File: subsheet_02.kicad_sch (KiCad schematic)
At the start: 1 part, among them J2 GATE_ARRAY_MO5_V1_SOCKET

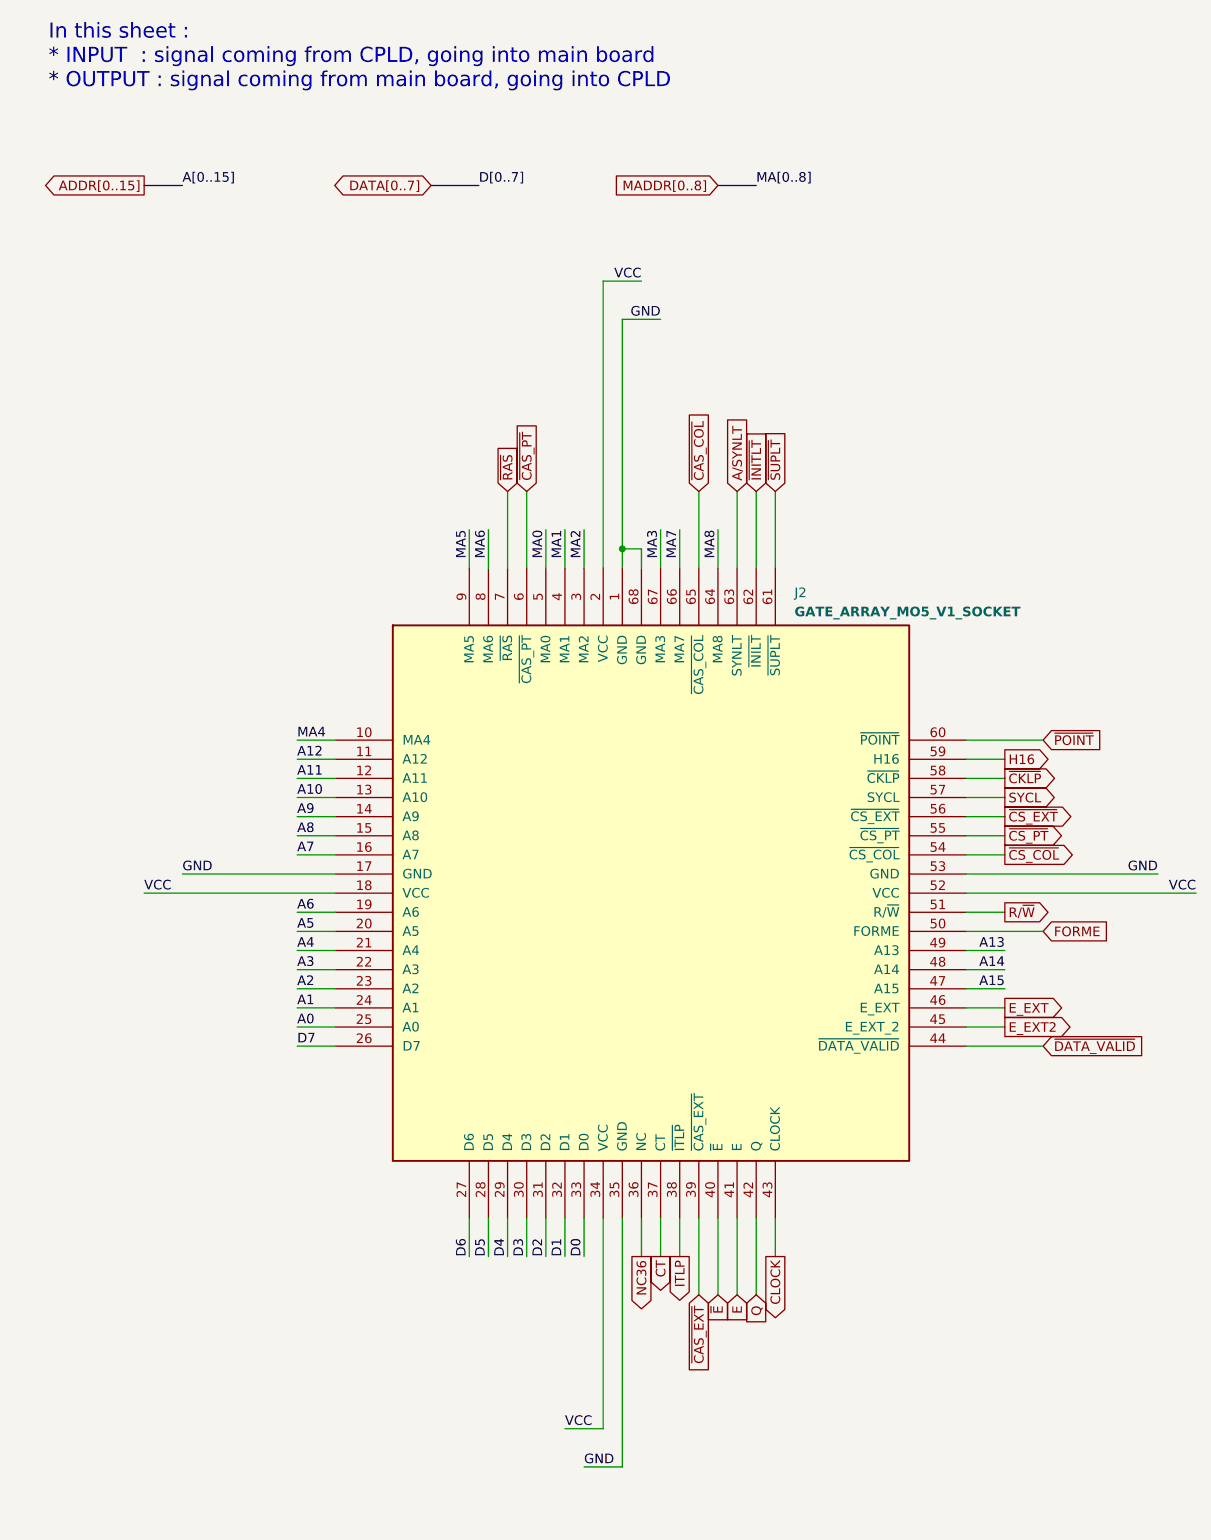
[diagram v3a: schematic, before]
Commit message: schematics : put power symbols
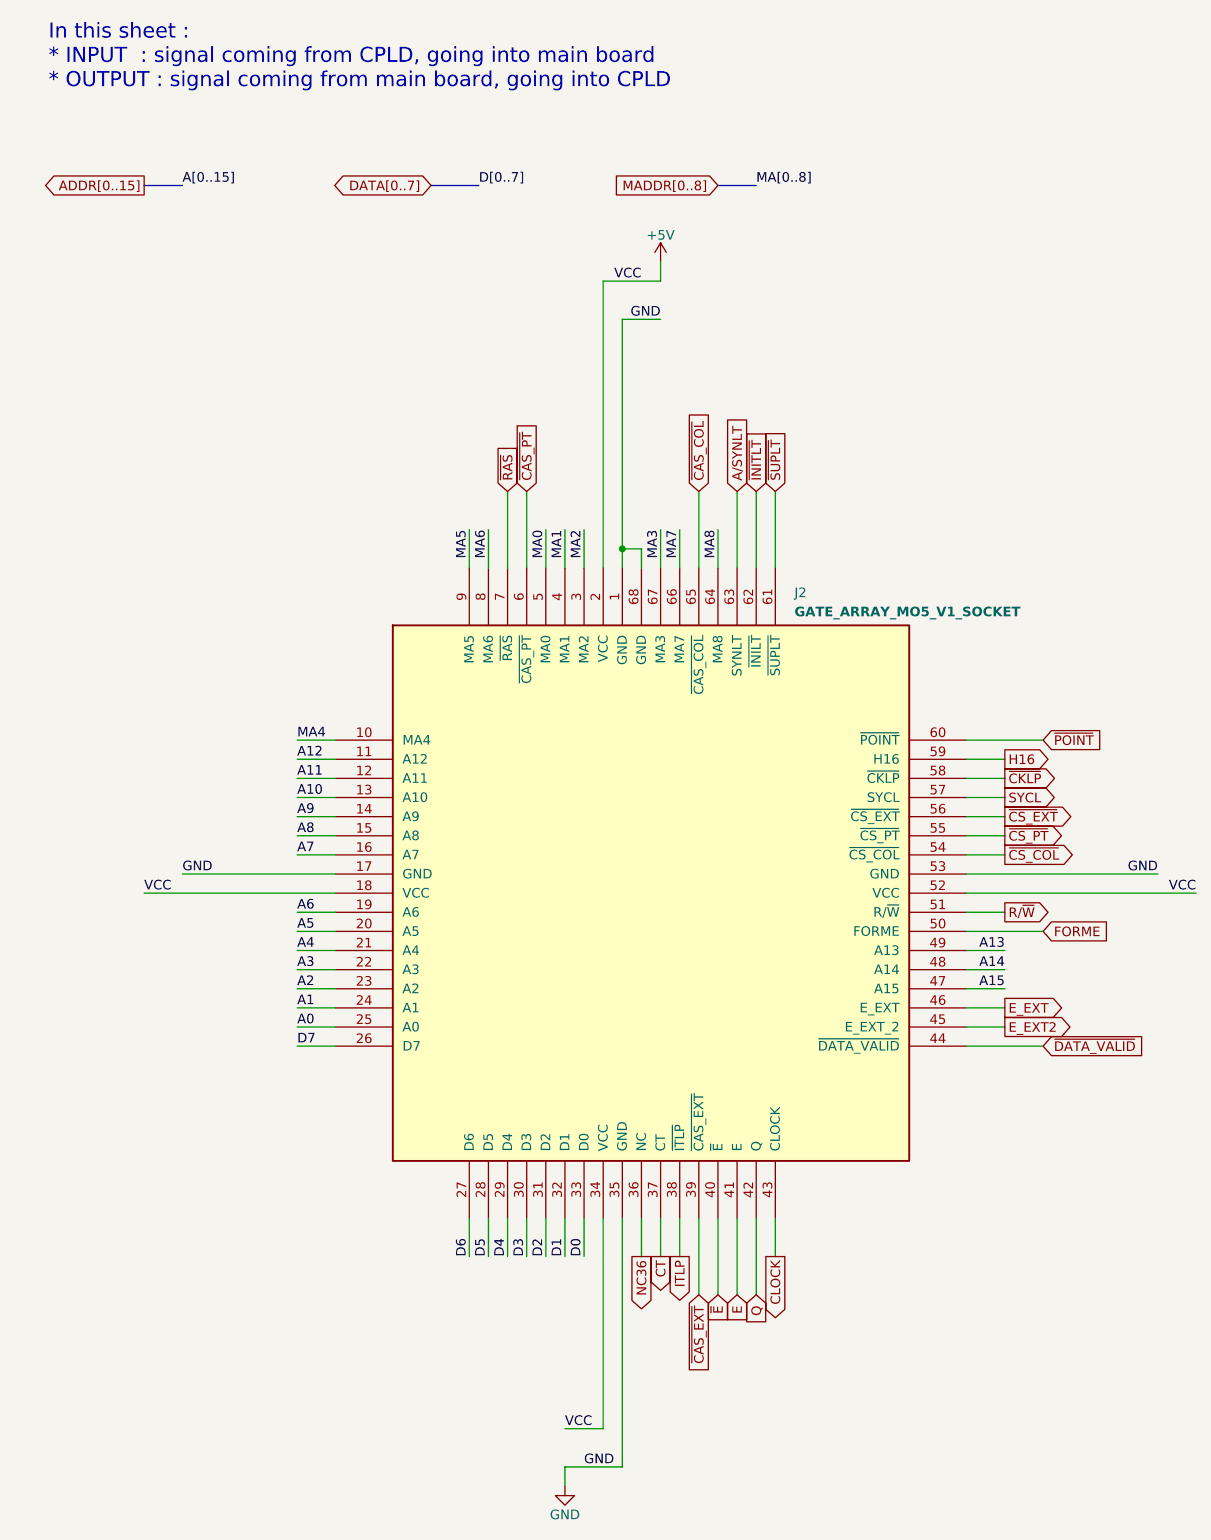
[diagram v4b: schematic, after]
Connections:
- net VCC renamed +5V
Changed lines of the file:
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@@
+    (stroke (width 0) (type default))
+  )
+  (wire (pts (xy 93.98 210.82) (xy 93.98 208.28))
     (stroke (width 0) (type default))
   )
@@
     (stroke (width 0) (type default))
   )
-  (wire (pts (xy 104.14 50.8) (xy 99.06 50.8))
+  (wire (pts (xy 99.06 50.8) (xy 106.68 50.8))
     (stroke (width 0) (type default))
   )
@@
     (stroke (width 0) (type default))
   )
-  (wire (pts (xy 96.52 208.28) (xy 101.6 208.28))
+  (wire (pts (xy 93.98 208.28) (xy 101.6 208.28))
     (stroke (width 0) (type default))
   )
@@
   )
   (wire (pts (xy 101.6 88.9) (xy 101.6 86.36))
+    (stroke (width 0) (type default))
+  )
+  (wire (pts (xy 106.68 48.26) (xy 106.68 50.8))
     (stroke (width 0) (type default))
   )
@@
     )
   )
+  (symbol (lib_id "power:+5V") (at 106.68 48.26 0) (unit 1)
+    (in_bom yes) (on_board yes) (dnp no)
+    (property "Reference" "#PWR02" (at 106.68 52.07 0)
+      (effects (font (size 1.27 1.27)) hide)
+    )
+    (property "Value" "+5V" (at 106.68 44.704 0)
+      (effects (font (size 1.27 1.27)))
+    )
+    (property "Footprint" "" (at 106.68 48.26 0)
+      (effects (font (size 1.27 1.27)) hide)
+    )
+    (property "Datasheet" "" (at 106.68 48.26 0)
+      (effects (font (size 1.27 1.27)) hide)
+    )
+    (pin "1")
+    (instances
+      (project "mo5-ga-motorola-repl--atf1508"
+        (path "/04881907-557f-4bbf-81fb-63c3424a1f56/2f3e2774-89af-48f0-a289-d0988ad66b48"
+          (reference "#PWR02") (unit 1)
+        )
+      )
+    )
+  )
+  (symbol (lib_id "power:GND") (at 93.98 210.82 0) (unit 1)
+    (in_bom yes) (on_board yes) (dnp no)
+    (property "Reference" "#PWR01" (at 93.98 217.17 0)
+      (effects (font (size 1.27 1.27)) hide)
+    )
+    (property "Value" "GND" (at 93.98 214.63 0)
+      (effects (font (size 1.27 1.27)))
+    )
+    (property "Footprint" "" (at 93.98 210.82 0)
+      (effects (font (size 1.27 1.27)) hide)
+    )
+    (property "Datasheet" "" (at 93.98 210.82 0)
+      (effects (font (size 1.27 1.27)) hide)
+    )
+    (pin "1")
+    (instances
+      (project "mo5-ga-motorola-repl--atf1508"
+        (path "/04881907-557f-4bbf-81fb-63c3424a1f56/2f3e2774-89af-48f0-a289-d0988ad66b48"
+          (reference "#PWR01") (unit 1)
+        )
+      )
+    )
+  )

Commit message: pcb : draft
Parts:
- J2: footprint Package_LCC:PLCC-68_THT-Socket -> SpecialConnectors:gate_array_plcc68_staggered
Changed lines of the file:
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@@
       (effects (font (size 1.27 1.27) bold) (justify left top))
     )
-    (property "Footprint" "Package_LCC:PLCC-68_THT-Socket" (at 124.46 88.9 0)
+    (property "Footprint" "SpecialConnectors:gate_array_plcc68_staggered" (at 124.46 88.9 0)
       (effects (font (size 1.27 1.27)) (justify left top) hide)
     )
